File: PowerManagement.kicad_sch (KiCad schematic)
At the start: 47 parts, among them Q15 NMOS, Q5 NMOS, Q6 NMOS, U12 OKI-78SR-3.3_1.5-W36H-C, U13 OKI-78SR-12_1.0-W36H-C, U14 MCP1501-30xSN, U18 LM393, U6 LM339

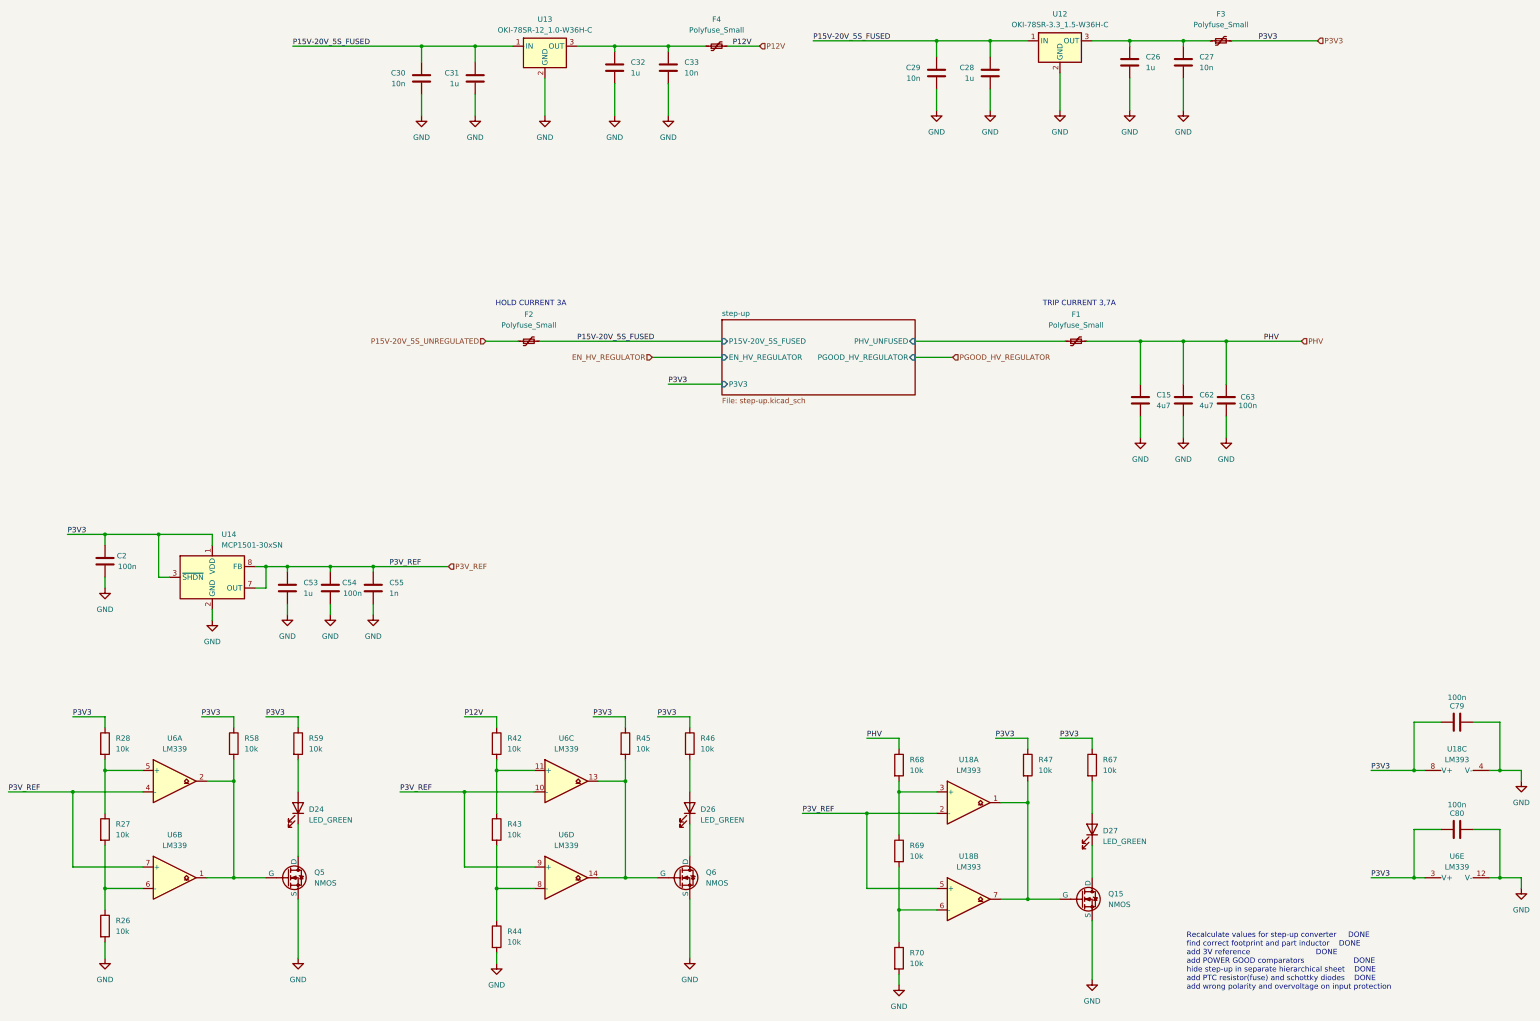
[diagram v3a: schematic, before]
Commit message: no errors schematic, basic routing done
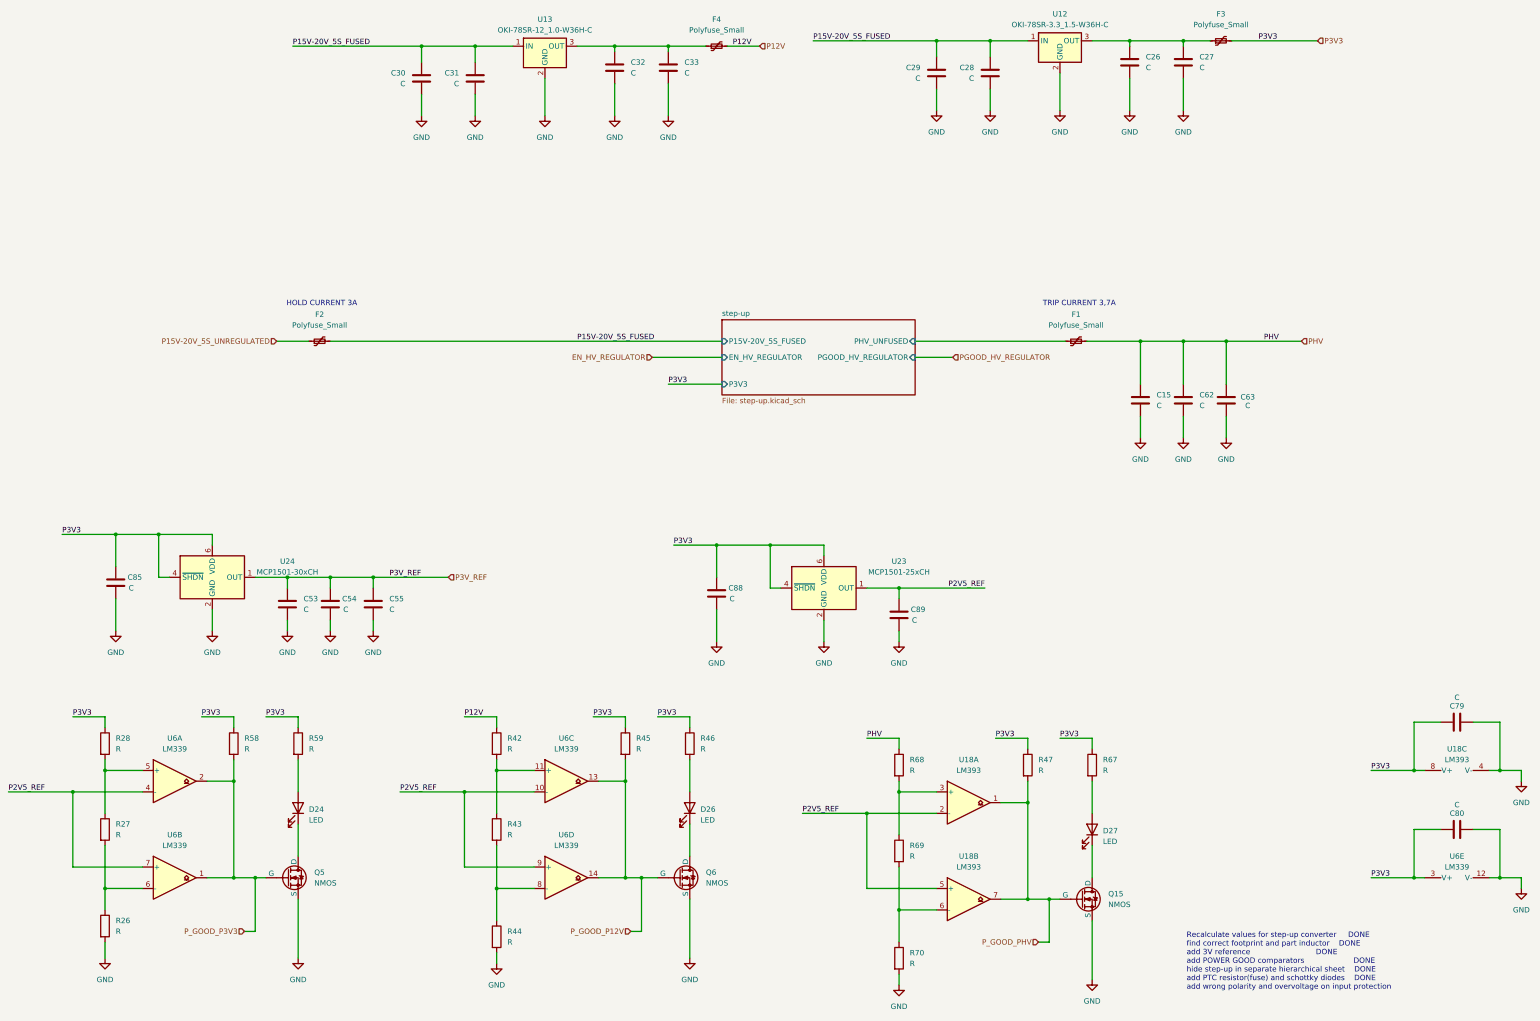
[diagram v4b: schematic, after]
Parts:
- removed C2: 100n, Capacitor_SMD:C_0603_1608Metric_Pad1.08x0.95mm_HandSolder, symbol Device:C
- removed U14: MCP1501-30xSN, Package_SO:SOIC-8_3.9x4.9mm_P1.27mm, symbol Reference_Voltage:MCP1501-30xSN
- added C85, C88, C89: C, Capacitor_SMD:C_0603_1608Metric_Pad1.08x0.95mm_HandSolder, symbol Device:C
- added U23: MCP1501-25xCH, Package_TO_SOT_SMD:SOT-23-6, symbol Reference_Voltage:MCP1501-25xCH
- added U24: MCP1501-30xCH, Package_TO_SOT_SMD:SOT-23-6, symbol Reference_Voltage:MCP1501-30xCH
- C15, C62: value 4u7 -> C
- C26, C28, C31, C32, C53: value 1u -> C
- C27, C29, C30, C33: value 10n -> C
- C54, C63, C79, C80: value 100n -> C
- C55: value 1n -> C
- D24, D26, D27: value LED_GREEN -> LED
- R26, R27, R28, R42, R43, R44, R45, R46, R47, R58, R59, R67, R68, R69, R70: value 10k -> R
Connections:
- net GND: now also C85.2, C88.2, C89.2, U23.2 (GND), U23.3 (GND), U23.5 (GND), U24.2 (GND), U24.3 (GND), U24.5 (GND)
- net P3V3: now also C85.1, C88.1, U23.4 (~{SHDN}), U23.6 (VDD), U24.4 (~{SHDN}), U24.6 (VDD)
- net P3V_REF: now also U24.1 (OUT); no longer U18.2 (-), U18.5 (+), U6.10 (-), U6.4 (-), U6.7 (+), U6.9 (+)
- net P_GOOD_P3V3: now reaches Q5.2 (G), R58.2, U6.1, U6.2
- net P_GOOD_PHV: now reaches Q15.2 (G), R47.2, U18.1, U18.7
- net P_GOOD_P12V: now reaches Q6.2 (G), R45.2, U6.13, U6.14
- new net P2V5_REF: C89.1, U18.2 (-), U18.5 (+), U23.1 (OUT), U6.10 (-), U6.4 (-), U6.7 (+), U6.9 (+)
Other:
- moved on the sheet: C53, C54, C55, F2

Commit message: DONE - before checking
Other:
- note added: "PWR Pins"
- note added: "Power OK comparators"
- note added: "Power supplies"
- note added: "Voltage references"
- moved on the sheet: C15, C26, C27, C28, C29, C30, C31, C32, C33, C53, C54, C55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

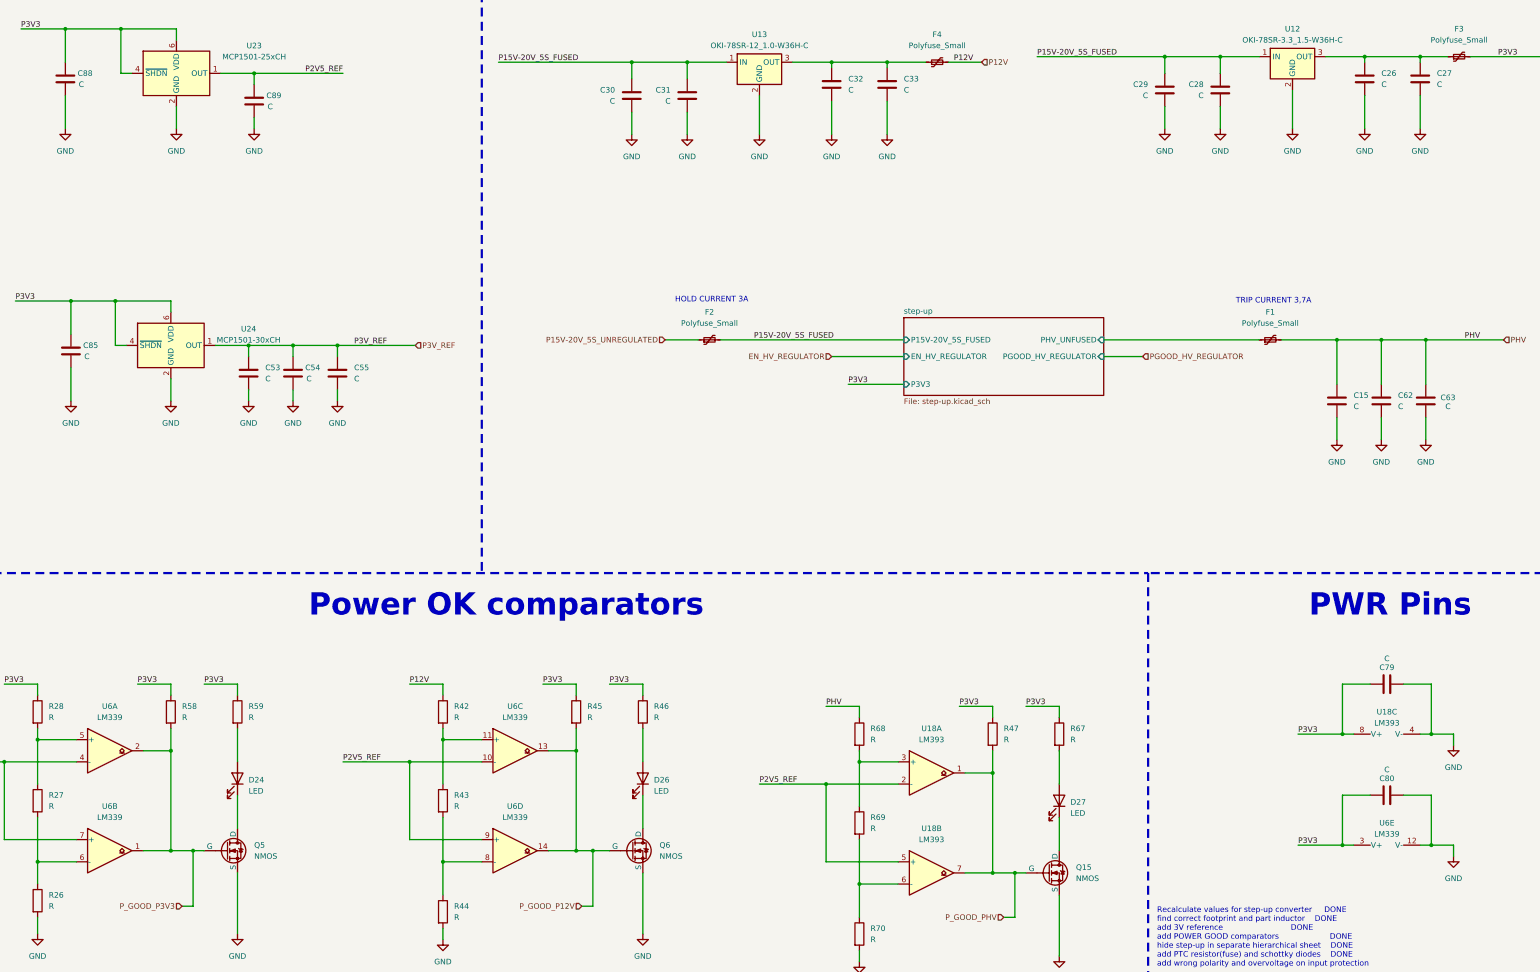
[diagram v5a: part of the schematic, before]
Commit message: most values in schematic filled corrected footprint mistake
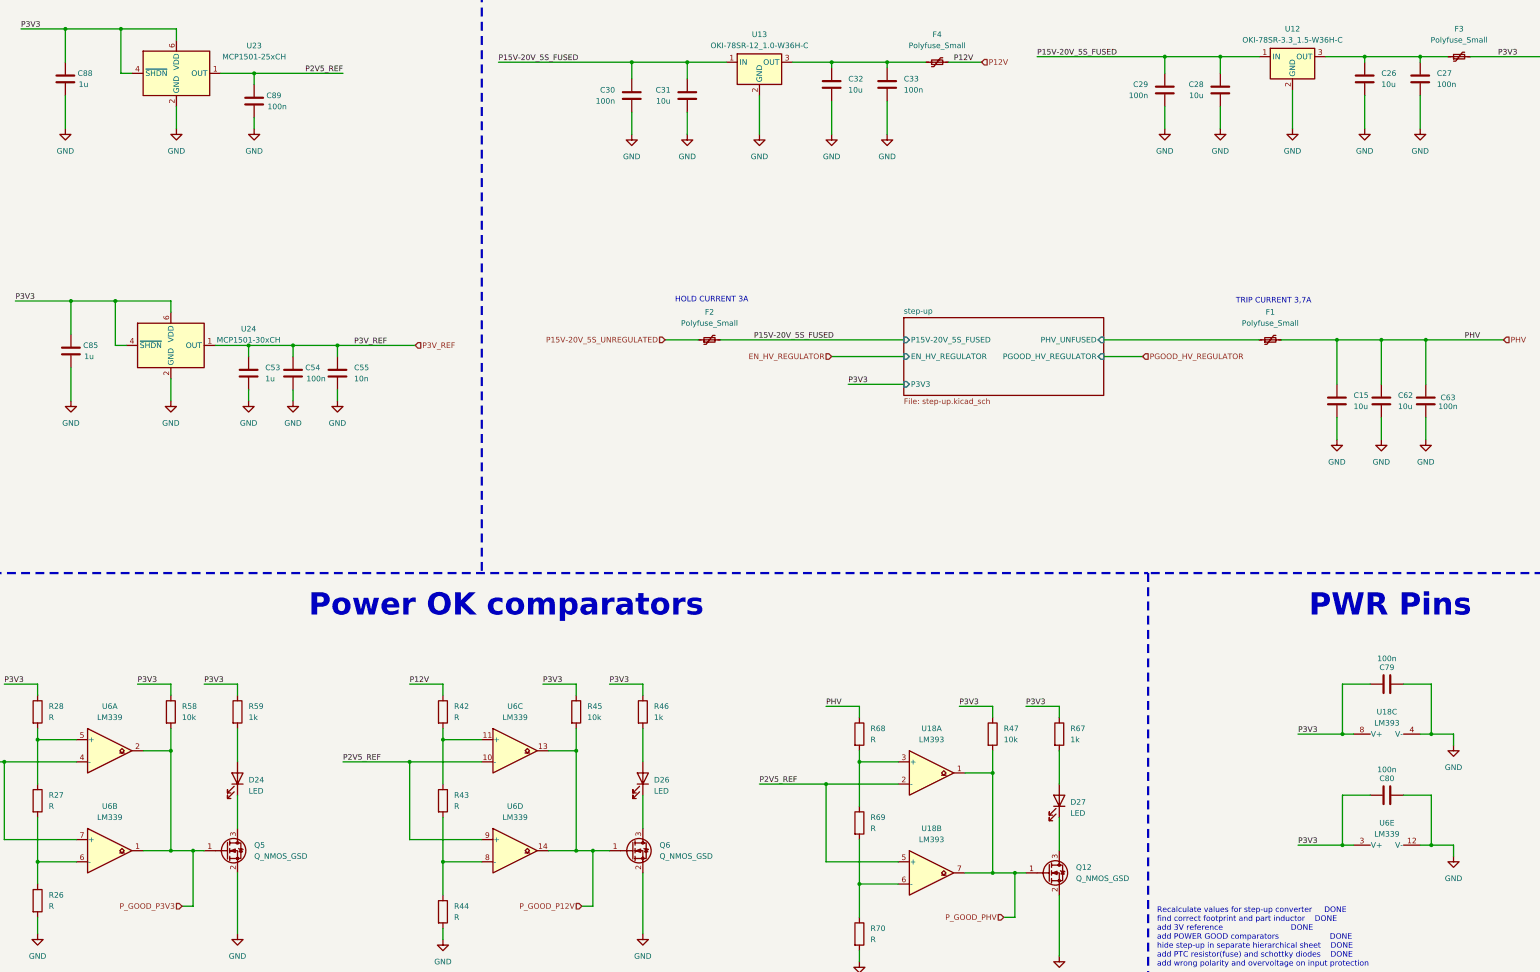
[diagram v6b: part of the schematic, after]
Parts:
- removed Q15, Q5, Q6: NMOS, Package_TO_SOT_SMD:SOT-23_Handsoldering, symbol Simulation_SPICE:NMOS
- added Q12, Q5, Q6: Q_NMOS_GSD, Package_TO_SOT_SMD:SOT-23_Handsoldering, symbol Device:Q_NMOS_GSD
- C15, C26, C28, C31, C32, C62: value C -> 10u
- C27, C29, C30, C33, C54, C63, C79, C80, C89: value C -> 100n
- C53: value C -> 1u
- C55: value C -> 10n
- C85, C88: value C -> 1u; footprint Capacitor_SMD:C_0603_1608Metric_Pad1.08x0.95mm_HandSolder -> Capacitor_SMD:C_0805_2012Metric_Pad1.18x1.45mm_HandSolder
- R45, R47, R58: value R -> 10k
- R46, R59, R67: value R -> 1k
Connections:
- net GND: now also Q12.2 (S), Q5.2 (S), Q6.2 (S)
- net P_GOOD_P12V: now also Q6.1 (G)
- net P_GOOD_P3V3: now also Q5.1 (G)
- net P_GOOD_PHV: now also Q12.1 (G)
- net at D24.1 (K): now also Q5.3 (D)
- net at D26.1 (K): now also Q6.3 (D)
- net at D27.1 (K): now also Q12.3 (D)

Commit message: V2 finished
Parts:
- removed C15, C62: 10u, Capacitor_SMD:C_0805_2012Metric_Pad1.18x1.45mm_HandSolder, symbol Device:C
- removed C53, C85: 1u, Capacitor_SMD:C_0805_2012Metric_Pad1.18x1.45mm_HandSolder, symbol Device:C
- removed C54, C63: 100n, Capacitor_SMD:C_0603_1608Metric_Pad1.08x0.95mm_HandSolder, symbol Device:C
- removed C55: 10n, Capacitor_SMD:C_0603_1608Metric_Pad1.08x0.95mm_HandSolder, symbol Device:C
- removed U24: MCP1501-30xCH, Package_TO_SOT_SMD:SOT-23-6, symbol Reference_Voltage:MCP1501-30xCH
- added D28: SML4740A-E3/61, Diode_SMD:D_SMA_Handsoldering, symbol Device:D_Zener
- added Q14: Q_PMOS_DGS, Package_TO_SOT_SMD:SOT-223-3_TabPin2, symbol Device:Q_PMOS_SDG
- added R17: 100k, Resistor_SMD:R_1206_3216Metric_Pad1.30x1.75mm_HandSolder, symbol Device:R
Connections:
- net GND: now also R17.1
- net P15V-20V_5S_UNREGULATED: now also Q14.2 (D); no longer F2.1
- net P3V3_UNFUSED: now reaches C26.2, C27.1, F3.1, U12.3 (OUT)
- net P12V_UNFUSED: now reaches C32.2, C33.1, F4.1, U13.3 (OUT)
- new net: D28.1 (K), F2.1, Q14.1 (S)
- new net: D28.2 (A), Q14.3 (G), R17.2
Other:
- moved on the sheet: F2
